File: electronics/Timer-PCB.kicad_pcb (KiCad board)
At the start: 2 copper layers, 5 parts

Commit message: init first version of PCB
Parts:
- removed G***: LOGO, Logos_k:K_Logo_31x7mm_KiCad_k
- added C1: 120n, Capacitor_THT_k:C_Axial_L5.1mm_D3.1mm_P7.50mm_Horizontal_k, F.Cu at (105.4, 102.9)
- added C2: 2200uF, Capacitor_THT_k:CP_Radial_D13.0mm_P5.00mm_k, F.Cu at (88.9, 127.0)
- added C3: 220uF, Capacitor_THT_k:CP_Radial_D8.0mm_P3.50mm_k, F.Cu at (129.7, 125.1)
- added D1: D_Bridge_+-AA, Diode_THT_k:Diode_Bridge_Round_D8.9mm_k, F.Cu at (77.5, 121.9)
- added D2: LED, LED_THT_k:LED_D5.0mm_Clear_k, F.Cu at (116.8, 90.8)
- added J1: Screw_Terminal_01x02, TerminalBlock_Phoenix_k:TerminalBlock_Phoenix_PT-1,5-2-3.5-H_1x02_P3.50mm_Horizontal_k, F.Cu at (69.8, 123.2)
- added J2: Screw_Terminal_01x03, TerminalBlock_Phoenix_k:TerminalBlock_Phoenix_PT-1,5-3-3.5-H_1x03_P3.50mm_Horizontal_k, F.Cu at (148.6, 126.3)
- added R1: R120, Resistor_THT_k:R_Axial_DIN0207_L6.3mm_D2.5mm_P10.16mm_Horizontal_k, F.Cu at (130.8, 102.9)
- added R2: 2k2, Resistor_THT_k:R_Axial_DIN0207_L6.3mm_D2.5mm_P10.16mm_Horizontal_k, F.Cu at (116.8, 106.7)
- added SW1: Rotary_Encoder_Switch, Rotary_Encoder_k:RotaryEncoder_Alps_EC11E-Switch_Vertical_H20mm_CircularMountingHoles_k, F.Cu at (134.6, 99.1)
- added U1: L7805, Package_TO_SOT_THT_k:TO-220-3_Horizontal_TabDown_k, F.Cu at (119.4, 129.5)
- added U2: Teensy-LC, Teensy.pretty:Teensy30_31_32_LC, F.Cu at (83.8, 102.9)
- added U3: 7-Seg_8dig_MAX7219, Display_7Segment_k:7seg_8dig_MAX7219_module, F.Cu at (107.0, 82.0)
- moved MH201 177.5 mm to (62.0, 74.0)
- moved MH202 163.1 mm to (62.0, 132.2)
- moved MH203 106.3 mm to (154.0, 74.0)
- moved MH204 80.0 mm to (154.0, 132.0)
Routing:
- net GND: track 0.00 -> 288.0 mm
- net +5V: track 0.00 -> 149.0 mm, vias 0 -> 2
- net VD: track 0.00 -> 77.6 mm
- net SSR: track 0.00 -> 72.1 mm, vias 0 -> 2
- net DIN: track 0.00 -> 70.5 mm
- net CLK: track 0.00 -> 64.4 mm, vias 0 -> 2
- net CS: track 0.00 -> 59.1 mm
- net Net-(SW1-PadA): track 0.00 -> 57.9 mm, vias 0 -> 2
- net Net-(SW1-PadB): track 0.00 -> 55.5 mm, vias 0 -> 2
- net Net-(C1-Pad2): track 0.00 -> 54.4 mm, vias 0 -> 2
- net Net-(R1-Pad1): track 0.00 -> 29.7 mm
- net Net-(D1-Pad3): track 0.00 -> 16.0 mm
- net Net-(D1-Pad4): track 0.00 -> 14.3 mm
- net Net-(D2-Pad2): track 0.00 -> 3.17 mm
- added copper zone on B.Cu, net GND
- added copper zone on F.Cu, net GND
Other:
- board outline added: 100 x 66 mm
- net class Default: clearance 0.2 -> 0.4
- rule trace_clearance: 0.2 -> 0.4
- board text added: "Timer PCB by Felix Piela"

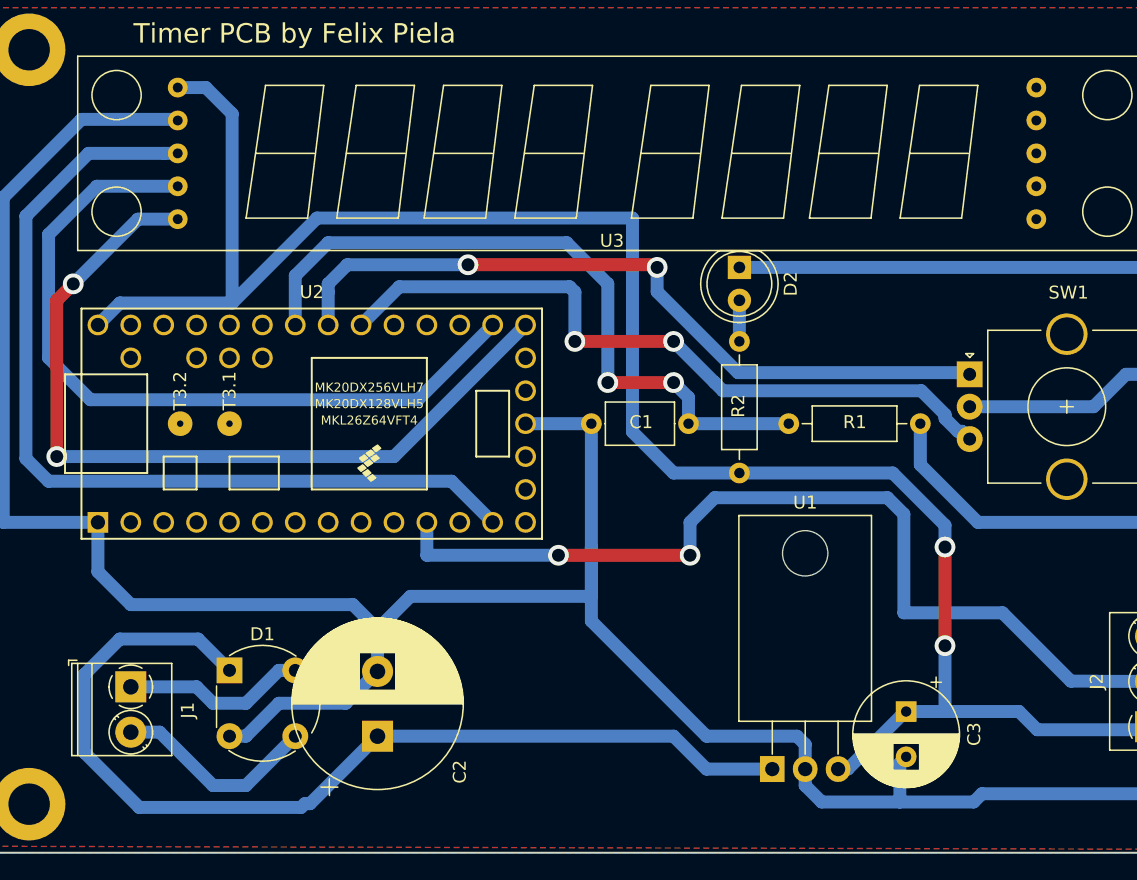
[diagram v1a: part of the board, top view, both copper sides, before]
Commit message: changed incorrect footprints (see #1)
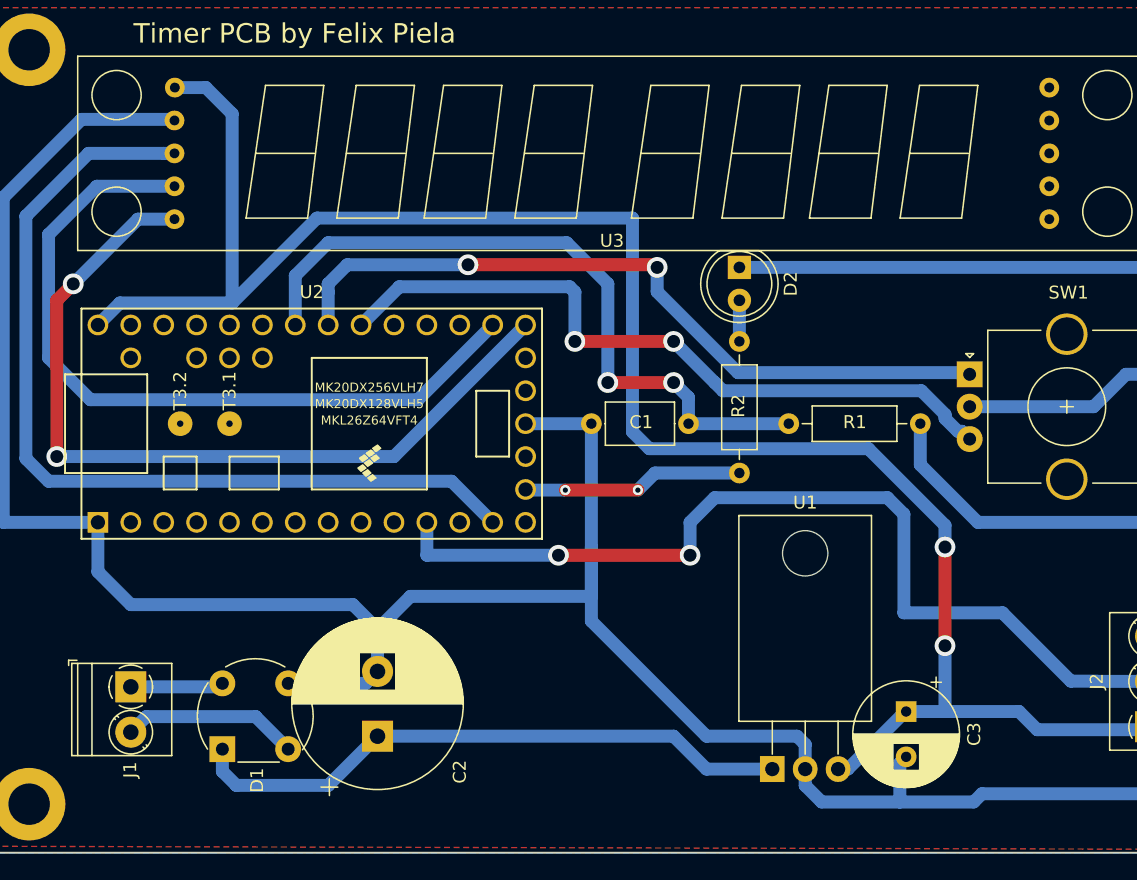
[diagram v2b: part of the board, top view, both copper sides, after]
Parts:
- D1: footprint Diode_THT_k:Diode_Bridge_Round_D8.9mm_k -> Diode_THT_k:Diode_Bridge_Round_D8.9mm_k_Segor_80C1500
- moved D1 6.10 mm to (76.9, 128.0), turned to 90 degrees
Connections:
- R2 pad 1: +5V -> Net-(R2-Pad1)
- U2 pad 15: Net-(U2-Pad15) -> Net-(R2-Pad1)
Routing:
- net VD: track 77.6 -> 47.3 mm
- net Net-(R2-Pad1): track 0.00 -> 17.1 mm, vias 0 -> 2
- net Net-(D1-Pad4): track 14.3 -> 7.18 mm
- net GND: track 288.0 -> 281.7 mm
- net Net-(D1-Pad3): track 16.0 -> 13.7 mm

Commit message: description on J2, see #2
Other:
- board text added: "+5V"
- board text added: "GND"
- board text added: "SW"

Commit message: thermal relieves improved, see #4, ground planes redrawn
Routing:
- removed copper zone on F.Cu, net GND
